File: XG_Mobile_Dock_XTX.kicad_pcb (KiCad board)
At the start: 8 copper layers, 220.1 x 123 mm, 144 parts, among them J1 5-1775443-8, J10 SWD, J11 UART, J12 I2C1, J13 39301240, J14 I2C1, J15 469911008, J2 20455-040E-76, J3 20455-040E-76, J5 USB_C_Receptacle, Q16 AO3401A, Q17 2N7002W, SW1 SW_Push, U1 DS320PR810NJXR, U12 STM32F030C8Tx, U2 DS320PR810NJXR

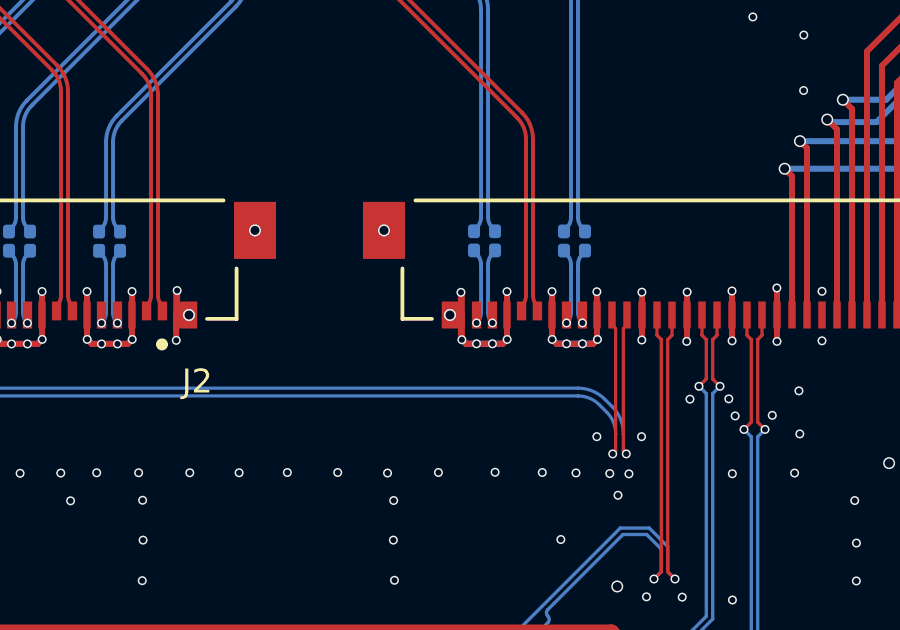
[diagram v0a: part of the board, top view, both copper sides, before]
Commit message: fixed wrong net classes
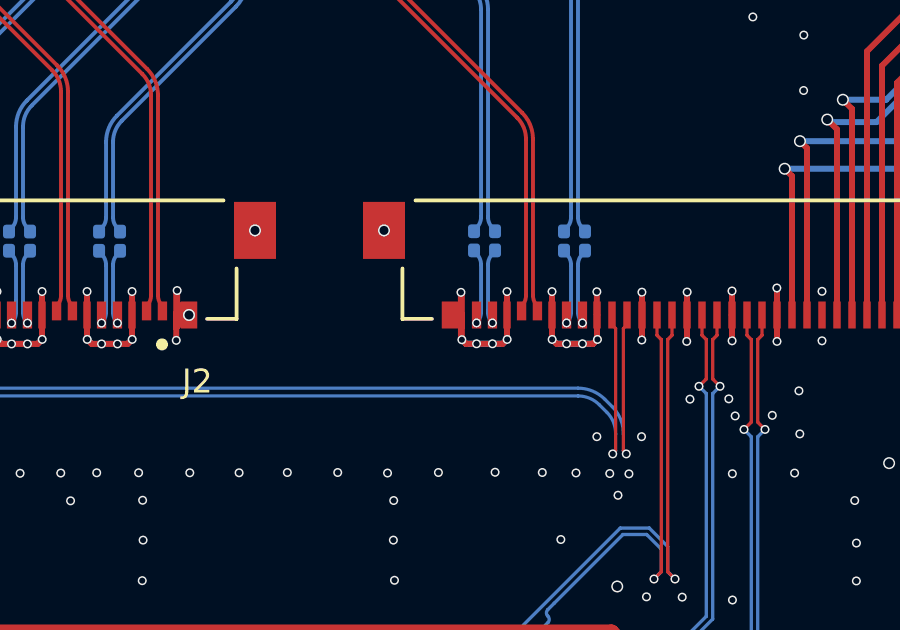
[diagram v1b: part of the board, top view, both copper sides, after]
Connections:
- J10 pad 1: +3V3 -> +3V3MCU
- J11 pad 1: +3V3 -> +3V3MCU
- R19 pad 1: +3V3 -> +3V3MCU
- R20 pad 1: +3V3 -> +3V3MCU
- R33 pad 1: +3V3 -> +3V3MCU
- R34 pad 1: +3V3 -> +3V3MCU
- R86 pad 2: +3V3 -> +3V3MCU
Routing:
- net +3V3MCU: track 54.5 -> 58.5 mm, vias 12 -> 15
- net +3V3: track 109.0 -> 105.1 mm, vias 33 -> 30
- net GND: vias 1035 -> 1034
